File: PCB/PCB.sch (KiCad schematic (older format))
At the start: 133 parts, among them J1 Conn_01x04, Q1 S8550, U1 Hx711

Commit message: Minor pcb modifications
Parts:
- removed C? (x11): 0.01U, Capacitor_SMD:C_0201_0603Metric_Pad0.64x0.40mm_HandSolder, symbol Device:C
- removed C? (x33): 1U, Capacitor_SMD:C_0201_0603Metric_Pad0.64x0.40mm_HandSolder, symbol Device:C
- removed Q? (x11): S8550, Package_TO_SOT_SMD:SC-59_Handsoldering, symbol Transistor_BJT:S8550
- removed R? (x11): 20K, Resistor_SMD:R_0402_1005Metric_Pad0.72x0.64mm_HandSolder, symbol Device:R
- removed R? (x11): 8.2K, Resistor_SMD:R_0402_1005Metric_Pad0.72x0.64mm_HandSolder, symbol Device:R
- removed R? (x11): 1k, Resistor_SMD:R_0402_1005Metric_Pad0.72x0.64mm_HandSolder, symbol Device:R
- removed TP? (x11): SG+, Connector_Wire:SolderWire-0.75sqmm_1x01_D1.25mm_OD2.3mm_Relief, symbol Connector:TestPoint
- removed TP? (x11): SG-, Connector_Wire:SolderWire-0.75sqmm_1x01_D1.25mm_OD2.3mm_Relief, symbol Connector:TestPoint
- removed U? (x11): Hx711, Package_SO:SOIC-16_3.9x9.9mm_P1.27mm, symbol HX711-ADC-rescue:Hx711-HX711
- added TP10, TP11, TP12, TP13, TP3, TP4, TP5, TP6, TP7, TP8, TP9: SG+, Custom-footprints:Radial-Pads-With-Relief, symbol Connector:TestPoint
- added TP14, TP15, TP16, TP17, TP18, TP19, TP20, TP21, TP22, TP23, TP24: SG-, Custom-footprints:Radial-Pads-With-Relief, symbol Connector:TestPoint
- TP1, TP2: footprint Connector_Wire:SolderWire-0.75sqmm_1x01_D1.25mm_OD2.3mm_Relief -> Custom-footprints:Radial-Pads-With-Relief
- renumbered C3 to C2, C4 to C3, C2 to C4
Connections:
- net at C1.2, R1.1: now also U1.8 (INA+)
- no-connect marks 36 -> 3
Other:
- moved on the sheet: C1, C2, C3, C4, Q1, R1, R2, R3, TP1, TP2, U1

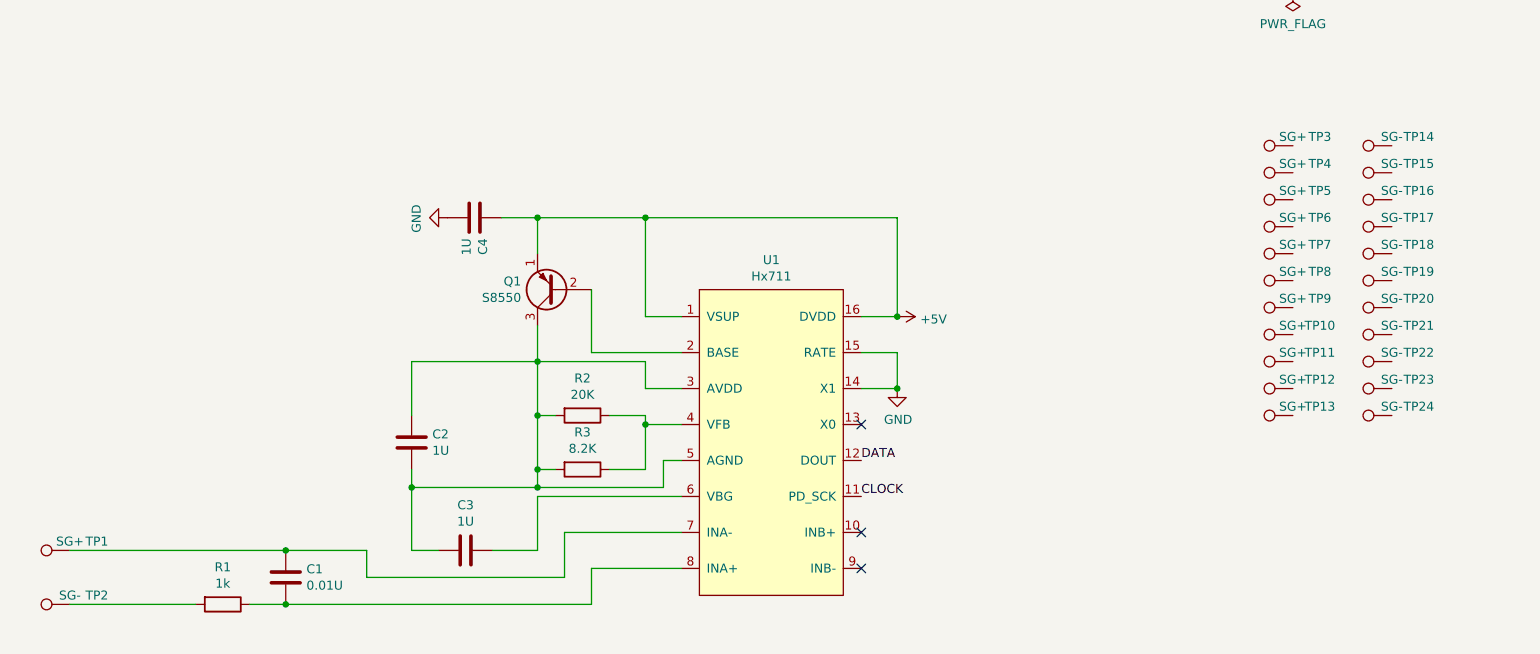
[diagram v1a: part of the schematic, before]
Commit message: More radial layout
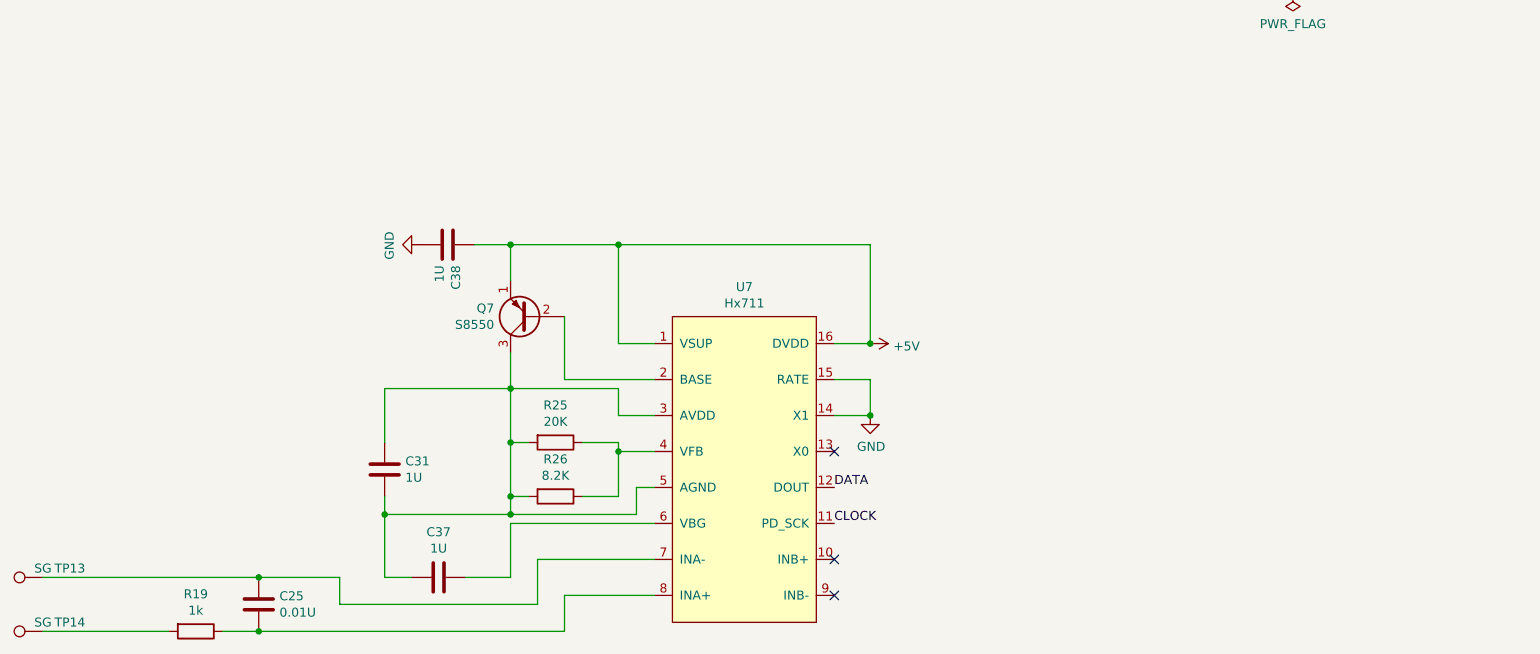
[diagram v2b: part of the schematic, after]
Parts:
- removed TP10, TP11, TP12, TP13, TP3, TP4, TP5, TP6, TP7, TP8, TP9: SG+, Custom-footprints:Radial-Pads-With-Relief, symbol Connector:TestPoint
- removed TP14, TP15, TP16, TP17, TP18, TP19, TP20, TP21, TP22, TP23, TP24: SG-, Custom-footprints:Radial-Pads-With-Relief, symbol Connector:TestPoint
- TP13: renamed from TP1; value SG+ -> SG
- TP14: renamed from TP2; value SG- -> SG
- renumbered C1 to C25, C2 to C31, C3 to C37, C4 to C38, Q1 to Q7, R1 to R19, R2 to R25, R3 to R26, U1 to U7
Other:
- moved on the sheet: C25, C31, C37, C38, Q7, R19, R25, R26, TP13, TP14, U7

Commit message: PCB
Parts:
- added C1, C17, C18, C19, C2, C20, C3, C34, C35, C36, C4: 0.01U, Capacitor_SMD:C_0201_0603Metric_Pad0.64x0.40mm_HandSolder, symbol Device:C
- added C10, C11, C12, C13, C14, C15, C16, C21, C22, C23, C24, C25, C26, C27, C28, C29, C30, C31, C32, C38, C39, C40, C42, C43, C44, C46, C47, C48, C5, C6, C7, C8, C9: 1U, Capacitor_SMD:C_0201_0603Metric_Pad0.64x0.40mm_HandSolder, symbol Device:C
- added Q1, Q10, Q11, Q12, Q2, Q3, Q4, Q5, Q6, Q7, Q8: S8550, Package_TO_SOT_SMD:SC-59_Handsoldering, symbol Transistor_BJT:S8550
- added R1, R13, R14, R15, R16, R2, R26, R27, R28, R3, R4: 1k, Resistor_SMD:R_0402_1005Metric_Pad0.72x0.64mm_HandSolder, symbol Device:R
- added R10, R12, R18, R20, R22, R24, R32, R34, R36, R6, R8: 8.2K, Resistor_SMD:R_0402_1005Metric_Pad0.72x0.64mm_HandSolder, symbol Device:R
- added R11, R17, R19, R21, R23, R31, R33, R35, R5, R7, R9: 20K, Resistor_SMD:R_0402_1005Metric_Pad0.72x0.64mm_HandSolder, symbol Device:R
- added TP1, TP10, TP11, TP12, TP13, TP14, TP15, TP16, TP19, TP2, TP20, TP21, TP22, TP23, TP24, TP3, TP4, TP5, TP6, TP7, TP8, TP9: SG, Custom-footprints:Radial-Pads-With-Relief, symbol Connector:TestPoint
- added TP25, TP26, TP27: 5V, Custom-footprints:Radial-Pads-With-Relief, symbol Connector:TestPoint
- added TP28, TP29, TP30: GND, Custom-footprints:Radial-Pads-With-Relief, symbol Connector:TestPoint
- added U1, U10, U11, U12, U2, U3, U4, U5, U6, U7, U8: Hx711, Package_SO:SOIC-16_3.9x9.9mm_P1.27mm, symbol HX711-ADC-rescue:Hx711-HX711
- renumbered C25 to C33, C31 to C37, C37 to C41, C38 to C45, Q7 to Q9, R19 to R25, R25 to R29, R26 to R30, TP13 to TP17, TP14 to TP18, U7 to U9
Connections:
- net +5V: now also C13.1, C14.1, C15.1, C16.1, C29.1, C30.1, C31.1, C32.1, C46.1, C47.1, C48.1, Q1.1 (E), Q10.1 (E), Q11.1 (E), Q12.1 (E), Q2.1 (E), Q3.1 (E), Q4.1 (E), Q5.1 (E), Q6.1 (E), Q7.1 (E), Q8.1 (E), U1.1 (VSUP), U1.16 (DVDD), U10.1 (VSUP), U10.16 (DVDD), U11.1 (VSUP), U11.16 (DVDD), U12.1 (VSUP), U12.16 (DVDD), U2.1 (VSUP), U2.16 (DVDD), U3.1 (VSUP), U3.16 (DVDD), U4.1 (VSUP), U4.16 (DVDD), U5.1 (VSUP), U5.16 (DVDD), U6.1 (VSUP), U6.16 (DVDD), U7.1 (VSUP), U7.16 (DVDD), U8.1 (VSUP), U8.16 (DVDD)
- net CLOCK: now also U1.11 (PD_SCK), U10.11 (PD_SCK), U11.11 (PD_SCK), U12.11 (PD_SCK), U2.11 (PD_SCK), U3.11 (PD_SCK), U4.11 (PD_SCK), U5.11 (PD_SCK), U6.11 (PD_SCK), U7.11 (PD_SCK), U8.11 (PD_SCK)
- net DATA: now also U1.12 (DOUT), U10.12 (DOUT), U11.12 (DOUT), U12.12 (DOUT), U2.12 (DOUT), U3.12 (DOUT), U4.12 (DOUT), U5.12 (DOUT), U6.12 (DOUT), U7.12 (DOUT), U8.12 (DOUT)
- net GND: now also C13.2, C14.2, C15.2, C16.2, C29.2, C30.2, C31.2, C32.2, C46.2, C47.2, C48.2, TP28.1, TP29.1, TP30.1, U1.14 (X1), U1.15 (RATE), U10.14 (X1), U10.15 (RATE), U11.14 (X1), U11.15 (RATE), U12.14 (X1), U12.15 (RATE), U2.14 (X1), U2.15 (RATE), U3.14 (X1), U3.15 (RATE), U4.14 (X1), U4.15 (RATE), U5.14 (X1), U5.15 (RATE), U6.14 (X1), U6.15 (RATE), U7.14 (X1), U7.15 (RATE), U8.14 (X1), U8.15 (RATE)
- new net: C34.1, TP19.1, U10.7 (INA-)
- new net: C34.2, R26.1, U10.8 (INA+)
- new net: C42.1, U10.6 (VBG)
- new net: C38.1, C38.2, C42.2, Q10.3 (C), R31.2, R32.2, U10.3 (AVDD), U10.5 (AGND)
- new net: R31.1, R32.1, U10.4 (VFB)
- new net: Q10.2 (B), U10.2 (BASE)
- new net: R26.2, TP20.1
- new net: C35.1, TP21.1, U11.7 (INA-)
- new net: C35.2, R27.1, U11.8 (INA+)
- new net: C43.1, U11.6 (VBG)
- new net: C39.1, C39.2, C43.2, Q11.3 (C), R33.2, R34.2, U11.3 (AVDD), U11.5 (AGND)
- new net: R33.1, R34.1, U11.4 (VFB)
- new net: Q11.2 (B), U11.2 (BASE)
- new net: R27.2, TP22.1
- new net: C36.1, TP23.1, U12.7 (INA-)
- new net: C36.2, R28.1, U12.8 (INA+)
- new net: C44.1, U12.6 (VBG)
- new net: C40.1, C40.2, C44.2, Q12.3 (C), R35.2, R36.2, U12.3 (AVDD), U12.5 (AGND)
- new net: R35.1, R36.1, U12.4 (VFB)
- new net: Q12.2 (B), U12.2 (BASE)
- new net: R28.2, TP24.1
- new net: C17.1, TP9.1, U5.7 (INA-)
- new net: C17.2, R13.1, U5.8 (INA+)
- new net: C25.1, U5.6 (VBG)
- new net: C21.1, C21.2, C25.2, Q5.3 (C), R17.2, R18.2, U5.3 (AVDD), U5.5 (AGND)
- new net: R17.1, R18.1, U5.4 (VFB)
- new net: Q5.2 (B), U5.2 (BASE)
- new net: R13.2, TP10.1
- new net: C18.1, TP11.1, U6.7 (INA-)
- new net: C18.2, R14.1, U6.8 (INA+)
- new net: C26.1, U6.6 (VBG)
- new net: C22.1, C22.2, C26.2, Q6.3 (C), R19.2, R20.2, U6.3 (AVDD), U6.5 (AGND)
- new net: R19.1, R20.1, U6.4 (VFB)
- new net: Q6.2 (B), U6.2 (BASE)
- new net: R14.2, TP12.1
- new net: C19.1, TP13.1, U7.7 (INA-)
- new net: C19.2, R15.1, U7.8 (INA+)
- new net: C27.1, U7.6 (VBG)
- new net: C23.1, C23.2, C27.2, Q7.3 (C), R21.2, R22.2, U7.3 (AVDD), U7.5 (AGND)
- new net: R21.1, R22.1, U7.4 (VFB)
- new net: Q7.2 (B), U7.2 (BASE)
- new net: R15.2, TP14.1
- new net: C20.1, TP15.1, U8.7 (INA-)
- new net: C20.2, R16.1, U8.8 (INA+)
- new net: C28.1, U8.6 (VBG)
- new net: C24.1, C24.2, C28.2, Q8.3 (C), R23.2, R24.2, U8.3 (AVDD), U8.5 (AGND)
- new net: R23.1, R24.1, U8.4 (VFB)
- new net: Q8.2 (B), U8.2 (BASE)
- new net: R16.2, TP16.1
- new net: C1.1, TP1.1, U1.7 (INA-)
- new net: C1.2, R1.1, U1.8 (INA+)
- new net: C9.1, U1.6 (VBG)
- new net: C5.1, C5.2, C9.2, Q1.3 (C), R5.2, R6.2, U1.3 (AVDD), U1.5 (AGND)
- new net: R5.1, R6.1, U1.4 (VFB)
- new net: Q1.2 (B), U1.2 (BASE)
- new net: R1.2, TP2.1
- new net: C2.1, TP3.1, U2.7 (INA-)
- new net: C2.2, R2.1, U2.8 (INA+)
- new net: C10.1, U2.6 (VBG)
- new net: C10.2, C6.1, C6.2, Q2.3 (C), R7.2, R8.2, U2.3 (AVDD), U2.5 (AGND)
- new net: R7.1, R8.1, U2.4 (VFB)
- new net: Q2.2 (B), U2.2 (BASE)
- new net: R2.2, TP4.1
- new net: C3.1, TP5.1, U3.7 (INA-)
- new net: C3.2, R3.1, U3.8 (INA+)
- new net: C11.1, U3.6 (VBG)
- new net: C11.2, C7.1, C7.2, Q3.3 (C), R10.2, R9.2, U3.3 (AVDD), U3.5 (AGND)
- new net: R10.1, R9.1, U3.4 (VFB)
- new net: Q3.2 (B), U3.2 (BASE)
- new net: R3.2, TP6.1
- new net: C4.1, TP7.1, U4.7 (INA-)
- new net: C4.2, R4.1, U4.8 (INA+)
- new net: C12.1, U4.6 (VBG)
- new net: C12.2, C8.1, C8.2, Q4.3 (C), R11.2, R12.2, U4.3 (AVDD), U4.5 (AGND)
- new net: R11.1, R12.1, U4.4 (VFB)
- new net: Q4.2 (B), U4.2 (BASE)
- new net: R4.2, TP8.1
- new net: TP25.1, TP26.1, TP27.1
- no-connect marks 3 -> 36
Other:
- moved on the sheet: C33, C37, C41, C45, Q9, R25, R29, R30, TP17, TP18, U9

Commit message: PCB
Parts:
- added H1, H2, H3, H4: MountingHole, MountingHole:MountingHole_5.5mm, symbol Mechanical:MountingHole
- C1, C10, C11, C12, C13, C14, C15, C16, C17, C18, C19, C2, C20, C21, C22, C23, C24, C25, C26, C27, C28, C29, C3, C30, C31, C32, C33, C34, C35, C36, C37, C38, C39, C4, C40, C41, C42, C43, C44, C45, C46, C47, C48, C5, C6, C7, C8, C9: footprint Capacitor_SMD:C_0201_0603Metric_Pad0.64x0.40mm_HandSolder -> Custom-footprints:C_0805_2012Metric_Pad1.18x1.45mm_HandSolder
- R1, R10, R11, R12, R13, R14, R15, R16, R17, R18, R19, R2, R20, R21, R22, R23, R24, R25, R26, R27, R28, R29, R3, R30, R31, R32, R33, R34, R35, R36, R4, R5, R6, R7, R8, R9: footprint Resistor_SMD:R_0402_1005Metric_Pad0.72x0.64mm_HandSolder -> Custom-footprints:R_0805_2012Metric_Pad1.20x1.40mm_HandSolder
